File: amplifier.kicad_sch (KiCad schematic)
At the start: 20 parts, among them U5 PAM8403D

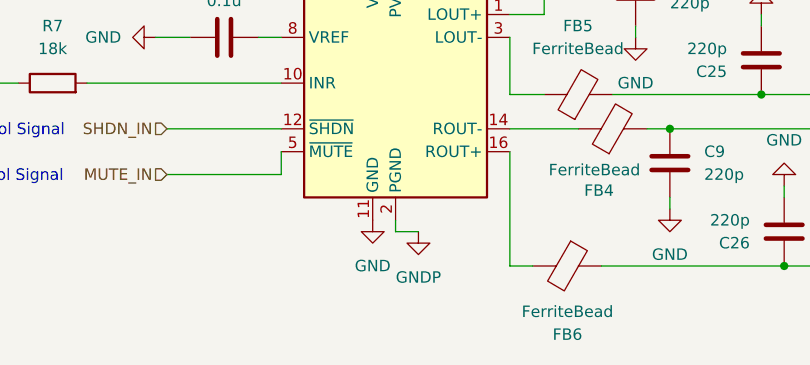
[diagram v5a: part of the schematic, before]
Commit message: PCB FINISHED - Gerber and drill files exported
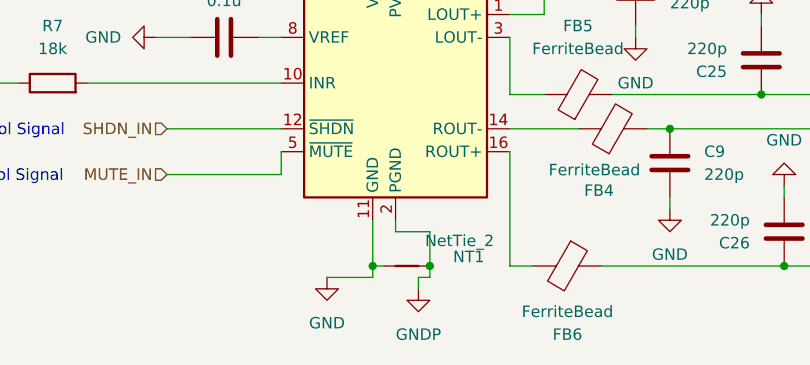
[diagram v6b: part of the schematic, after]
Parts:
- added NT1: NetTie_2, Net_Tie:Net_Tie_0.2, symbol Device:NetTie_2
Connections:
- net GND: now also NT1.1
- net GNDP: now also NT1.2
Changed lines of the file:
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@@
+	)
+	(junction
+		(at 138.43 113.03)
+		(diameter 0)
+		(color 0 0 0 0)
 	)
 	(junction
@@
 	)
 	(junction
+		(at 132.08 113.03)
+		(diameter 0)
+		(color 0 0 0 0)
+	)
+	(junction
 		(at 175.26 93.98)
 		(diameter 0)
@@
 		)
 	)
+	(wire
+		(pts
+			(xy 138.43 113.03) (xy 138.43 109.22)
+		)
+		(stroke
+			(width 0)
+			(type default)
+		)
+	)
 	(polyline
 		(pts
@@
 	(wire
 		(pts
+			(xy 137.16 114.3) (xy 138.43 114.3)
+		)
+		(stroke
+			(width 0)
+			(type default)
+		)
+	)
+	(wire
+		(pts
 			(xy 184.15 113.03) (xy 177.8 113.03)
 		)
@@
 	(wire
 		(pts
+			(xy 138.43 114.3) (xy 138.43 113.03)
+		)
+		(stroke
+			(width 0)
+			(type default)
+		)
+	)
+	(wire
+		(pts
 			(xy 132.08 62.23) (xy 129.54 62.23)
 		)
@@
 	(wire
 		(pts
+			(xy 132.08 107.95) (xy 132.08 113.03)
+		)
+		(stroke
+			(width 0)
+			(type default)
+		)
+	)
+	(wire
+		(pts
 			(xy 134.62 109.22) (xy 134.62 107.95)
 		)
@@
 	(wire
 		(pts
+			(xy 132.08 114.3) (xy 132.08 113.03)
+		)
+		(stroke
+			(width 0)
+			(type default)
+		)
+	)
+	(wire
+		(pts
 			(xy 129.54 59.69) (xy 129.54 62.23)
 		)
@@
 	(wire
 		(pts
+			(xy 137.16 115.57) (xy 137.16 114.3)
+		)
+		(stroke
+			(width 0)
+			(type default)
+		)
+	)
+	(wire
+		(pts
+			(xy 127 114.3) (xy 132.08 114.3)
+		)
+		(stroke
+			(width 0)
+			(type default)
+		)
+	)
+	(wire
+		(pts
 			(xy 132.08 77.47) (xy 132.08 62.23)
 		)
@@
 	(wire
 		(pts
-			(xy 137.16 109.22) (xy 134.62 109.22)
+			(xy 134.62 109.22) (xy 138.43 109.22)
+		)
+		(stroke
+			(width 0)
+			(type default)
+		)
+	)
+	(wire
+		(pts
+			(xy 133.35 113.03) (xy 132.08 113.03)
 		)
 		(stroke
@@
 	)
 	(symbol
+		(lib_id "Device:NetTie_2")
+		(at 135.89 113.03 0)
+		(unit 1)
+		(exclude_from_sim no)
+		(in_bom no)
+		(on_board yes)
+		(dnp no)
+		(property "Reference" "NT1"
+			(at 142.748 112.014 0)
+			(effects
+				(font
+					(size 1.27 1.27)
+				)
+			)
+		)
+		(property "Value" "NetTie_2"
+			(at 141.732 110.236 0)
+			(effects
+				(font
+					(size 1.27 1.27)
+				)
+			)
+		)
+		(property "Footprint" "Net_Tie:Net_Tie_0.2"
+			(at 135.89 113.03 0)
+			(effects
+				(font
+					(size 1.27 1.27)
+				)
+				(hide yes)
+			)
+		)
+		(property "Datasheet" "~"
+			(at 135.89 113.03 0)
+			(effects
+				(font
+					(size 1.27 1.27)
+				)
+				(hide yes)
+			)
+		)
+		(property "Description" "Net tie, 2 pins"
+			(at 135.89 113.03 0)
+			(effects
+				(font
+					(size 1.27 1.27)
+				)
+				(hide yes)
+			)
+		)
+		(pin "2"
+		)
+		(pin "1"
+		)
+		(instances
+			(project "plant caretaker"
+				(path "/23b35dcc-615e-4aec-abee-c26cc3d8b906/64bd70cc-1431-45fc-8946-041e9631b1bb"
+					(reference "NT1")
+					(unit 1)
+				)
+			)
+		)
+	)
+	(symbol
 		(lib_id "Device:C_Polarized")
 		(at 146.05 62.23 0)
@@
 	(symbol
 		(lib_id "power:GND")
-		(at 137.16 109.22 0)
+		(at 137.16 115.57 0)
 		(unit 1)
 		(exclude_from_sim no)
@@
 		(fields_autoplaced yes)
 		(property "Reference" "#PWR011"
+			(at 137.16 121.92 0)
+			(effects
+				(font
+					(size 1.27 1.27)
+				)
+				(hide yes)
+			)
+		)
+		(property "Value" "GNDP"
+			(at 137.16 120.65 0)
+			(effects
+				(font
+					(size 1.27 1.27)
+				)
+			)
+		)
+		(property "Footprint" ""
 			(at 137.16 115.57 0)
 			(effects
@@
 			)
 		)
-		(property "Value" "GNDP"
-			(at 137.16 114.3 0)
-			(effects
-				(font
-					(size 1.27 1.27)
-				)
-			)
-		)
-		(property "Footprint" ""
-			(at 137.16 109.22 0)
-			(effects
-				(font
-					(size 1.27 1.27)
-				)
-				(hide yes)
-			)
-		)
 		(property "Datasheet" ""
-			(at 137.16 109.22 0)
+			(at 137.16 115.57 0)
 			(effects
 				(font
@@
 		)
 		(property "Description" "Power symbol creates a global label with name \"GND\" , ground"
-			(at 137.16 109.22 0)
+			(at 137.16 115.57 0)
 			(effects
 				(font
@@
 	(symbol
 		(lib_id "power:GND")
-		(at 132.08 107.95 0)
+		(at 127 114.3 0)
 		(unit 1)
 		(exclude_from_sim no)
@@
 		(fields_autoplaced yes)
 		(property "Reference" "#PWR015"
-			(at 132.08 114.3 0)
+			(at 127 120.65 0)
 			(effects
 				(font
@@
 		)
 		(property "Value" "GND"
-			(at 132.08 113.03 0)
+			(at 127 119.38 0)
 			(effects
 				(font
@@
 		)
 		(property "Footprint" ""
-			(at 132.08 107.95 0)
+			(at 127 114.3 0)
 			(effects
 				(font
@@
 		)
 		(property "Datasheet" ""
-			(at 132.08 107.95 0)
+			(at 127 114.3 0)
 			(effects
 				(font
@@
 		)
 		(property "Description" "Power symbol creates a global label with name \"GND\" , ground"
-			(at 132.08 107.95 0)
-			(effects
-				(font
+			(at 127 114.3 0)
+			(effects
+				(font
